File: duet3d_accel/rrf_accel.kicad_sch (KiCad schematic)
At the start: 13 parts, among them J1 Conn_02x05_Odd_Even, U1 LIS3DH

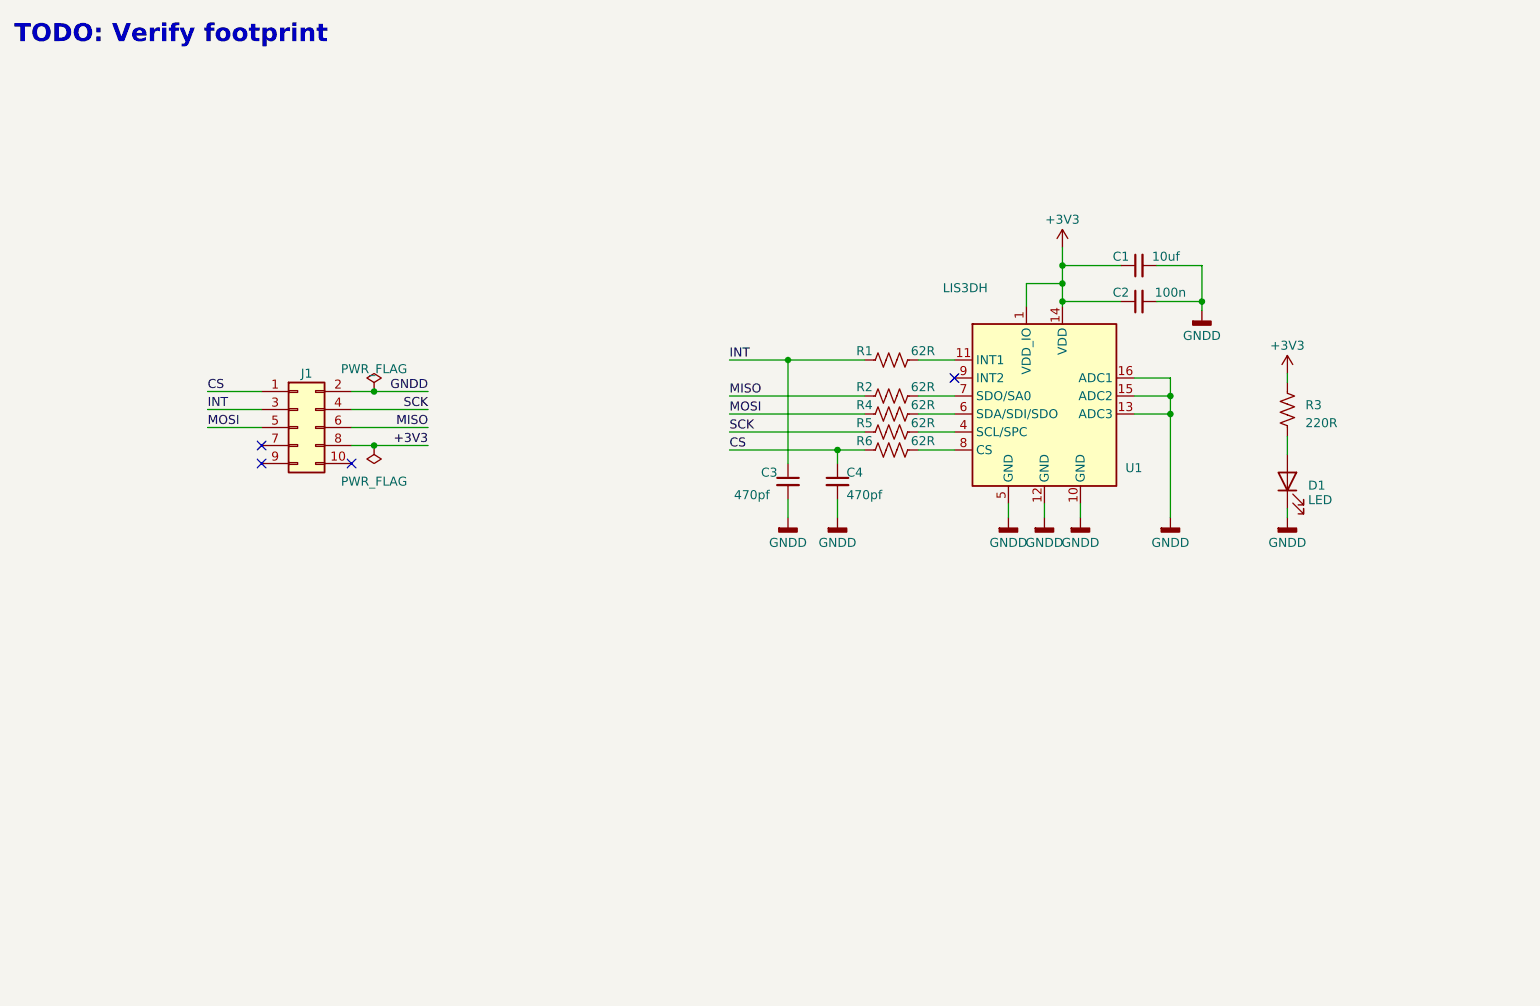
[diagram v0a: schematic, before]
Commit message: Renamed libraries
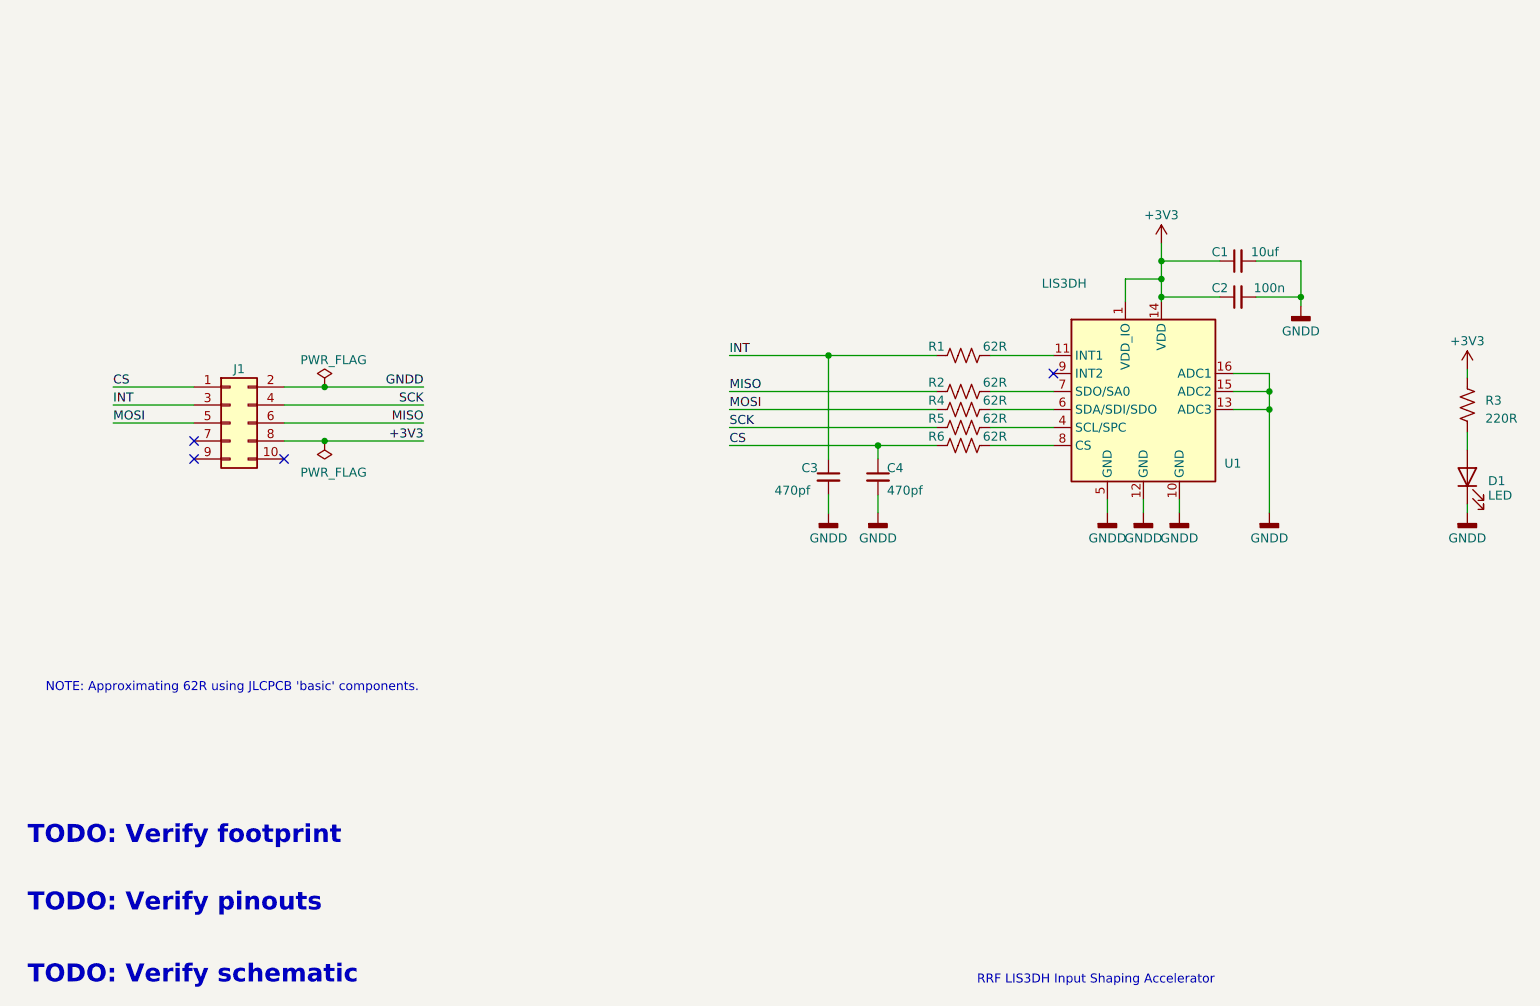
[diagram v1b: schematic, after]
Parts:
- J1: footprint duet3d_accel:PinHeader_2x05_P2.54mm_Vertical_SMD -> rrf_accel:PinHeader_2x05_P2.54mm_Vertical_SMD
- U1: footprint duet3d_accel:LGA-16_3x3mm_P0.5mm_LayoutBorder3x5y -> rrf_accel:LGA-16_3x3mm_P0.5mm_LayoutBorder3x5y; symbol duet3d_accel:LIS3DH -> rrf_accel:LIS3DH
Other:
- note added: "NOTE: Approximating 62R using JLCPCB 'basic' components."
- note added: "RRF LIS3DH Input Shaping Accelerator"
- note added: "TODO: Verify pinouts"
- note added: "TODO: Verify schematic"
- moved on the sheet: C1, C2, C3, C4, D1, J1, R1, R2, R3, R4, R5, R6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

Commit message: Fixed schematic.
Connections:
- net CS: no longer C4.1
- net at R6.2, U1.8 (CS): now also C4.1
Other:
- note added: "TODO: Verify JLCPCB componnent values and sizes."
- note removed: "TODO: Verify pinouts"
- note removed: "TODO: Verify schematic"
- moved on the sheet: C4, R1, R2, R4, R5, R6

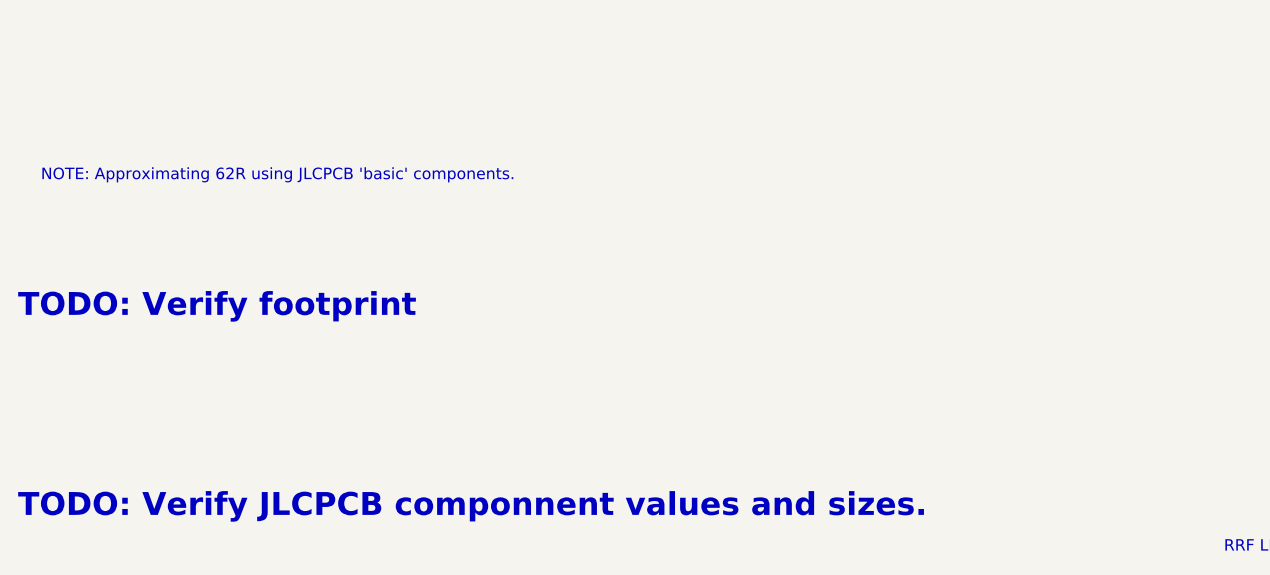
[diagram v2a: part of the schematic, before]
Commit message: Tweaked schematic and layout.
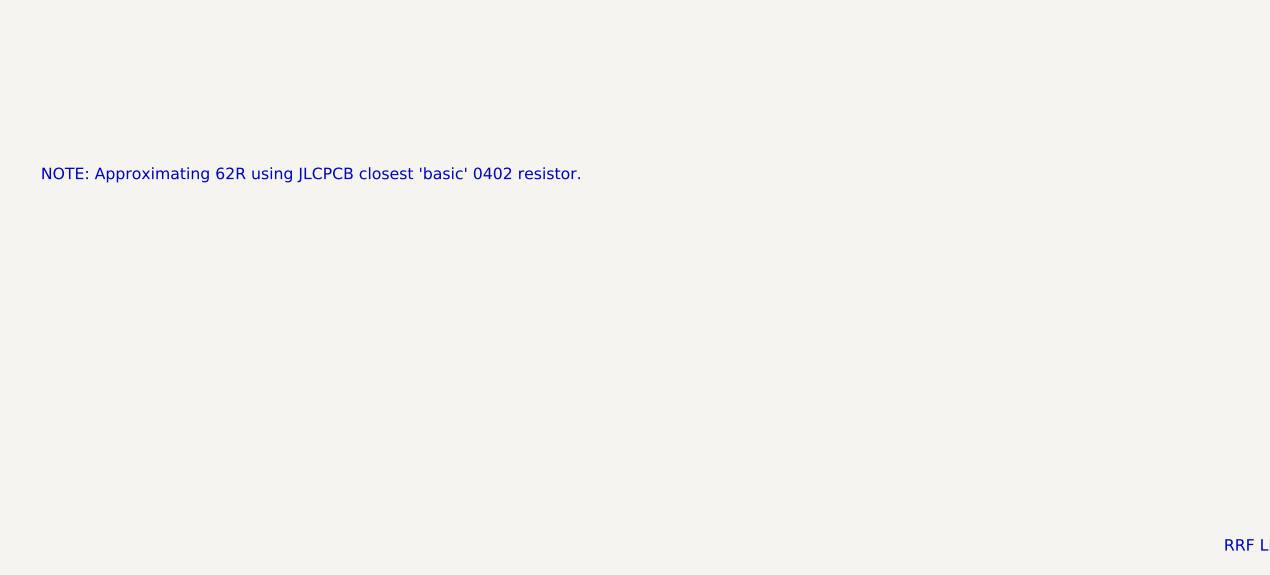
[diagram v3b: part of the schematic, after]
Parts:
- C1, C3, C4: footprint Capacitor_SMD:C_0603_1608Metric_Pad1.08x0.95mm_HandSolder -> Capacitor_SMD:C_0603_1608Metric
- C2: footprint Capacitor_SMD:C_0402_1005Metric_Pad0.74x0.62mm_HandSolder -> Capacitor_SMD:C_0402_1005Metric; LCSC C96446 -> C1525
- D1: footprint LED_SMD:LED_0603_1608Metric_Pad1.05x0.95mm_HandSolder -> LED_SMD:LED_0603_1608Metric
- R1, R2, R3, R4, R5, R6: footprint Resistor_SMD:R_0402_1005Metric_Pad0.72x0.64mm_HandSolder -> Resistor_SMD:R_0402_1005Metric
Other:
- note added: "NOTE: Approximating 62R using JLCPCB closest 'basic' 0402 resistor."
- note removed: "NOTE: Approximating 62R using JLCPCB 'basic' components."
- note removed: "TODO: Verify JLCPCB componnent values and sizes."
- note removed: "TODO: Verify footprint"
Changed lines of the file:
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@@
     (stroke (width 0) (type default))
   )
-  (text "TODO: Verify JLCPCB componnent values and sizes." (at 31.75 176.53 0)
-    (effects (font (size 2.54 2.54) (thickness 0.508) bold (color 255 0 0 1)) (justify left bottom))
-  )
   (text "RRF LIS3DH Input Shaping Accelerator" (at 165.735 180.34 0)
     (effects (font (size 1.27 1.27)) (justify left bottom))
   )
-  (text "TODO: Verify footprint" (at 31.75 154.305 0)
-    (effects (font (size 2.54 2.54) (thickness 0.508) bold (color 255 0 0 1)) (justify left bottom))
-  )
-  (text "NOTE: Approximating 62R using JLCPCB 'basic' components."
+  (text "NOTE: Approximating 62R using JLCPCB closest 'basic' 0402 resistor."
     (at 34.29 139.065 0)
     (effects (font (size 1.27 1.27)) (justify left bottom))
@@
       (effects (font (size 1.27 1.27)))
     )
-    (property "Footprint" "Resistor_SMD:R_0402_1005Metric_Pad0.72x0.64mm_HandSolder" (at 156.464 98.044 90)
+    (property "Footprint" "Resistor_SMD:R_0402_1005Metric" (at 156.464 98.044 90)
       (effects (font (size 1.27 1.27)) hide)
     )
@@
       (effects (font (size 1.27 1.27)) (justify left))
     )
-    (property "Footprint" "Resistor_SMD:R_0402_1005Metric_Pad0.72x0.64mm_HandSolder" (at 235.966 98.679 90)
+    (property "Footprint" "Resistor_SMD:R_0402_1005Metric" (at 235.966 98.679 90)
       (effects (font (size 1.27 1.27)) hide)
     )
@@
       (effects (font (size 1.27 1.27)) (justify left))
     )
-    (property "Footprint" "Capacitor_SMD:C_0603_1608Metric_Pad1.08x0.95mm_HandSolder" (at 167.005 108.585 0)
+    (property "Footprint" "Capacitor_SMD:C_0603_1608Metric" (at 167.005 108.585 0)
       (effects (font (size 1.27 1.27)) hide)
     )
@@
       (effects (font (size 1.27 1.27)))
     )
-    (property "Footprint" "Resistor_SMD:R_0402_1005Metric_Pad0.72x0.64mm_HandSolder" (at 156.464 90.424 90)
+    (property "Footprint" "Resistor_SMD:R_0402_1005Metric" (at 156.464 90.424 90)
       (effects (font (size 1.27 1.27)) hide)
     )
@@
       (effects (font (size 1.27 1.27)))
     )
-    (property "Footprint" "Resistor_SMD:R_0402_1005Metric_Pad0.72x0.64mm_HandSolder" (at 156.464 100.584 90)
+    (property "Footprint" "Resistor_SMD:R_0402_1005Metric" (at 156.464 100.584 90)
       (effects (font (size 1.27 1.27)) hide)
     )
@@
       (effects (font (size 1.27 1.27)))
     )
-    (property "Footprint" "Resistor_SMD:R_0402_1005Metric_Pad0.72x0.64mm_HandSolder" (at 156.464 103.124 90)
+    (property "Footprint" "Resistor_SMD:R_0402_1005Metric" (at 156.464 103.124 90)
       (effects (font (size 1.27 1.27)) hide)
     )
@@
       (effects (font (size 1.27 1.27)) (justify right))
     )
-    (property "Footprint" "LED_SMD:LED_0603_1608Metric_Pad1.05x0.95mm_HandSolder" (at 234.95 108.585 0)
+    (property "Footprint" "LED_SMD:LED_0603_1608Metric" (at 234.95 108.585 0)
       (effects (font (size 1.27 1.27)) hide)
     )
@@
       (effects (font (size 1.27 1.27)) (justify left))
     )
-    (property "Footprint" "Capacitor_SMD:C_0603_1608Metric_Pad1.08x0.95mm_HandSolder" (at 144.78 108.585 0)
+    (property "Footprint" "Capacitor_SMD:C_0603_1608Metric" (at 144.78 108.585 0)
       (effects (font (size 1.27 1.27)) hide)
     )
@@
       (effects (font (size 1.27 1.27)))
     )
-    (property "Footprint" "Resistor_SMD:R_0402_1005Metric_Pad0.72x0.64mm_HandSolder" (at 156.464 95.504 90)
+    (property "Footprint" "Resistor_SMD:R_0402_1005Metric" (at 156.464 95.504 90)
       (effects (font (size 1.27 1.27)) hide)
     )
@@
       (effects (font (size 1.27 1.27)))
     )
-    (property "Footprint" "Capacitor_SMD:C_0603_1608Metric_Pad1.08x0.95mm_HandSolder" (at 202.565 78.105 0)
+    (property "Footprint" "Capacitor_SMD:C_0603_1608Metric" (at 202.565 78.105 0)
       (effects (font (size 1.27 1.27)) hide)
     )
@@
       (effects (font (size 1.27 1.27)))
     )
-    (property "Footprint" "Capacitor_SMD:C_0402_1005Metric_Pad0.74x0.62mm_HandSolder" (at 202.565 83.185 0)
+    (property "Footprint" "Capacitor_SMD:C_0402_1005Metric" (at 202.565 83.185 0)
       (effects (font (size 1.27 1.27)) hide)
     )
@@
       (effects (font (size 1.27 1.27)) hide)
     )
-    (property "LCSC" "C96446" (at 202.565 83.185 0)
-      (effects (font (size 1.27 1.27)) hide)
-    )
+    (property "LCSC" "C1525" (at 202.565 83.185 0)
+      (effects (font (size 1.27 1.27)) hide)
+    )
